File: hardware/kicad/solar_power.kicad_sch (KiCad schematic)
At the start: 12 parts, among them U4 AEM10941

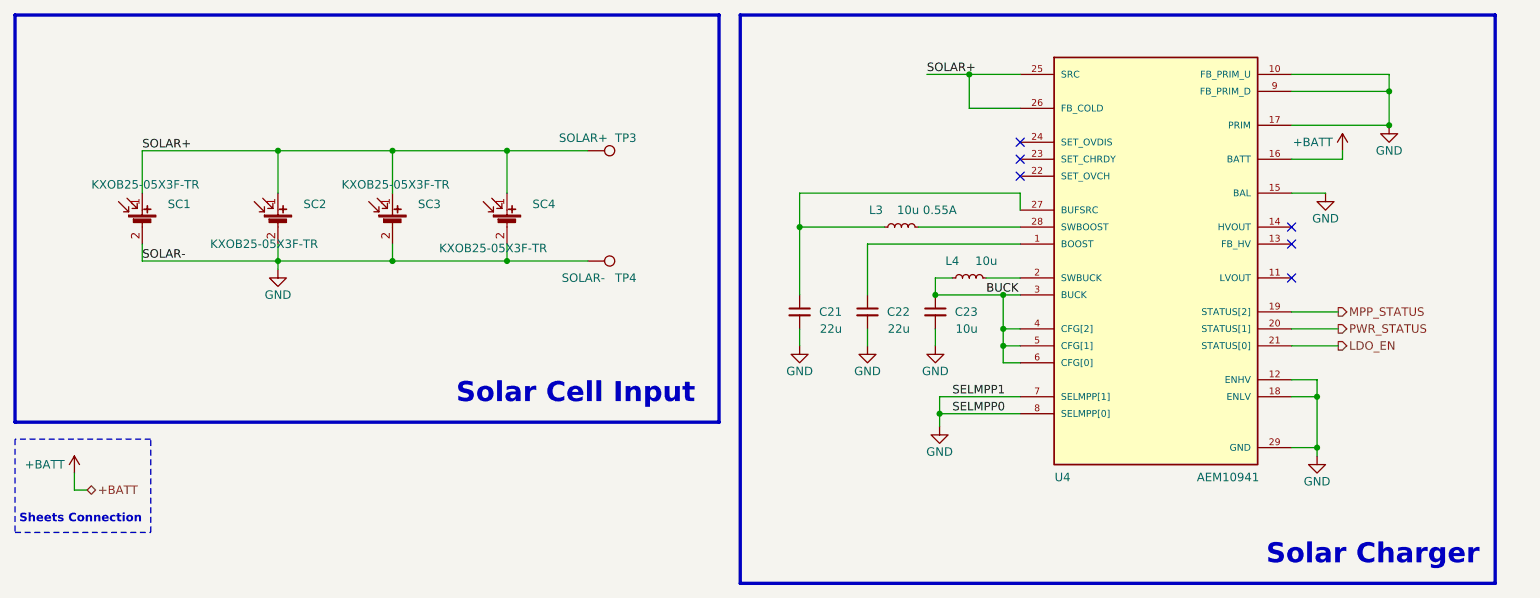
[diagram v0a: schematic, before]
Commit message: update schematics with gnss
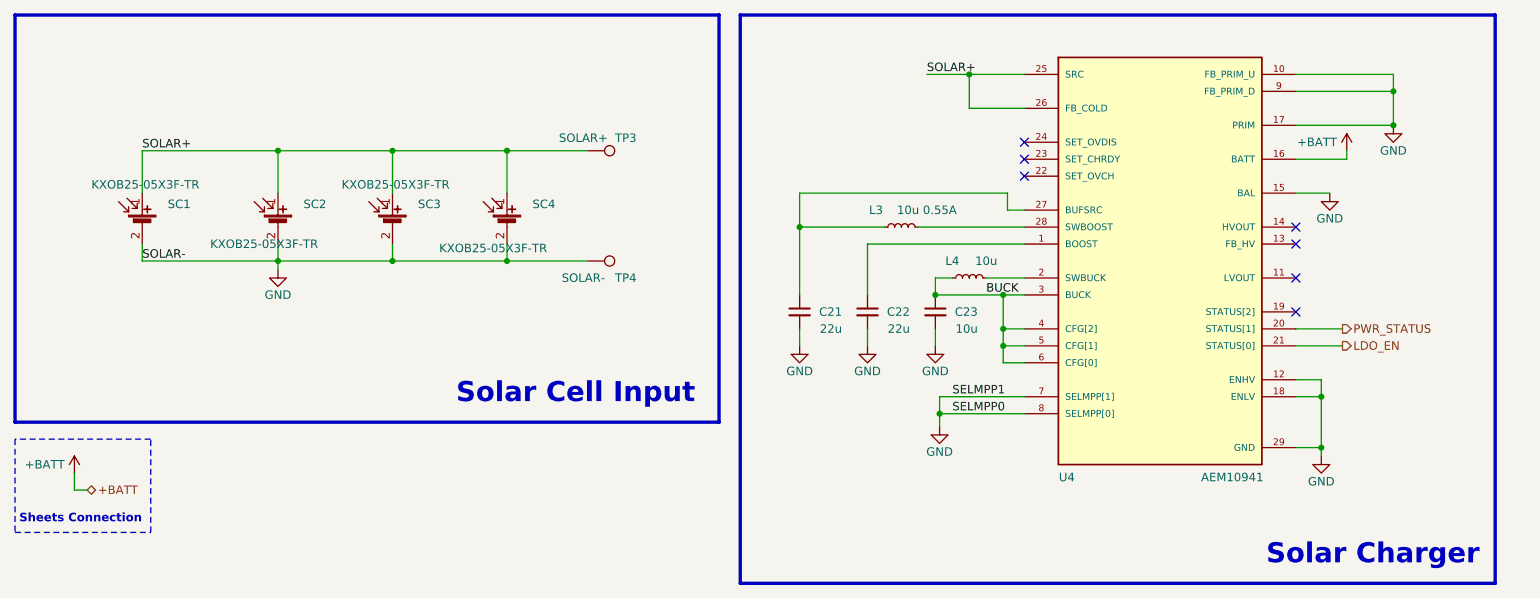
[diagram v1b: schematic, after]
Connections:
- net MPP_STATUS: no longer names the net of U4.19 (STATUS[2])
- no-connect marks 6 -> 7
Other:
- moved on the sheet: U4

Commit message: update schematics info
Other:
- title: Solar Power -> Teapotlabs Atlas
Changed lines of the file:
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@@
 	(paper "A4")
 	(title_block
-		(title "Solar Power")
-		(date "2024-04-06")
-		(rev "5")
+		(title "Teapotlabs Atlas")
+		(date "2024-10-25")
+		(rev "1")
 		(company "Teapot Laboratories")
 	)
